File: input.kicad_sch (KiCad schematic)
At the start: 3 parts, among them U8 PC817

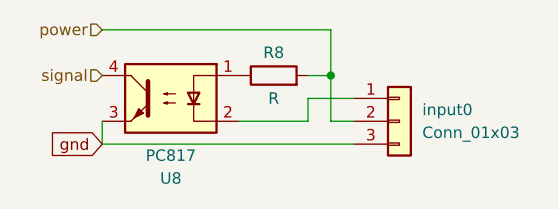
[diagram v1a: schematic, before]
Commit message: adding pullups to in1-3
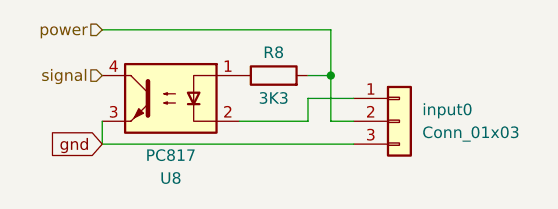
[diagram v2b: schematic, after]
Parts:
- R8: value R -> 3K3
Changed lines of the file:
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@@
       (effects (font (size 1.27 1.27)))
     )
-    (property "Value" "R" (at 135.89 87.63 90)
+    (property "Value" "3K3" (at 135.89 87.63 90)
       (effects (font (size 1.27 1.27)))
     )
